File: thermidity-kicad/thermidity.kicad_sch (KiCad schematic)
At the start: 14 parts, among them J1 Battery, J2 Display, J3 ISP, U1 ATmega328P, U2 HIH-5030, U3 TMP36

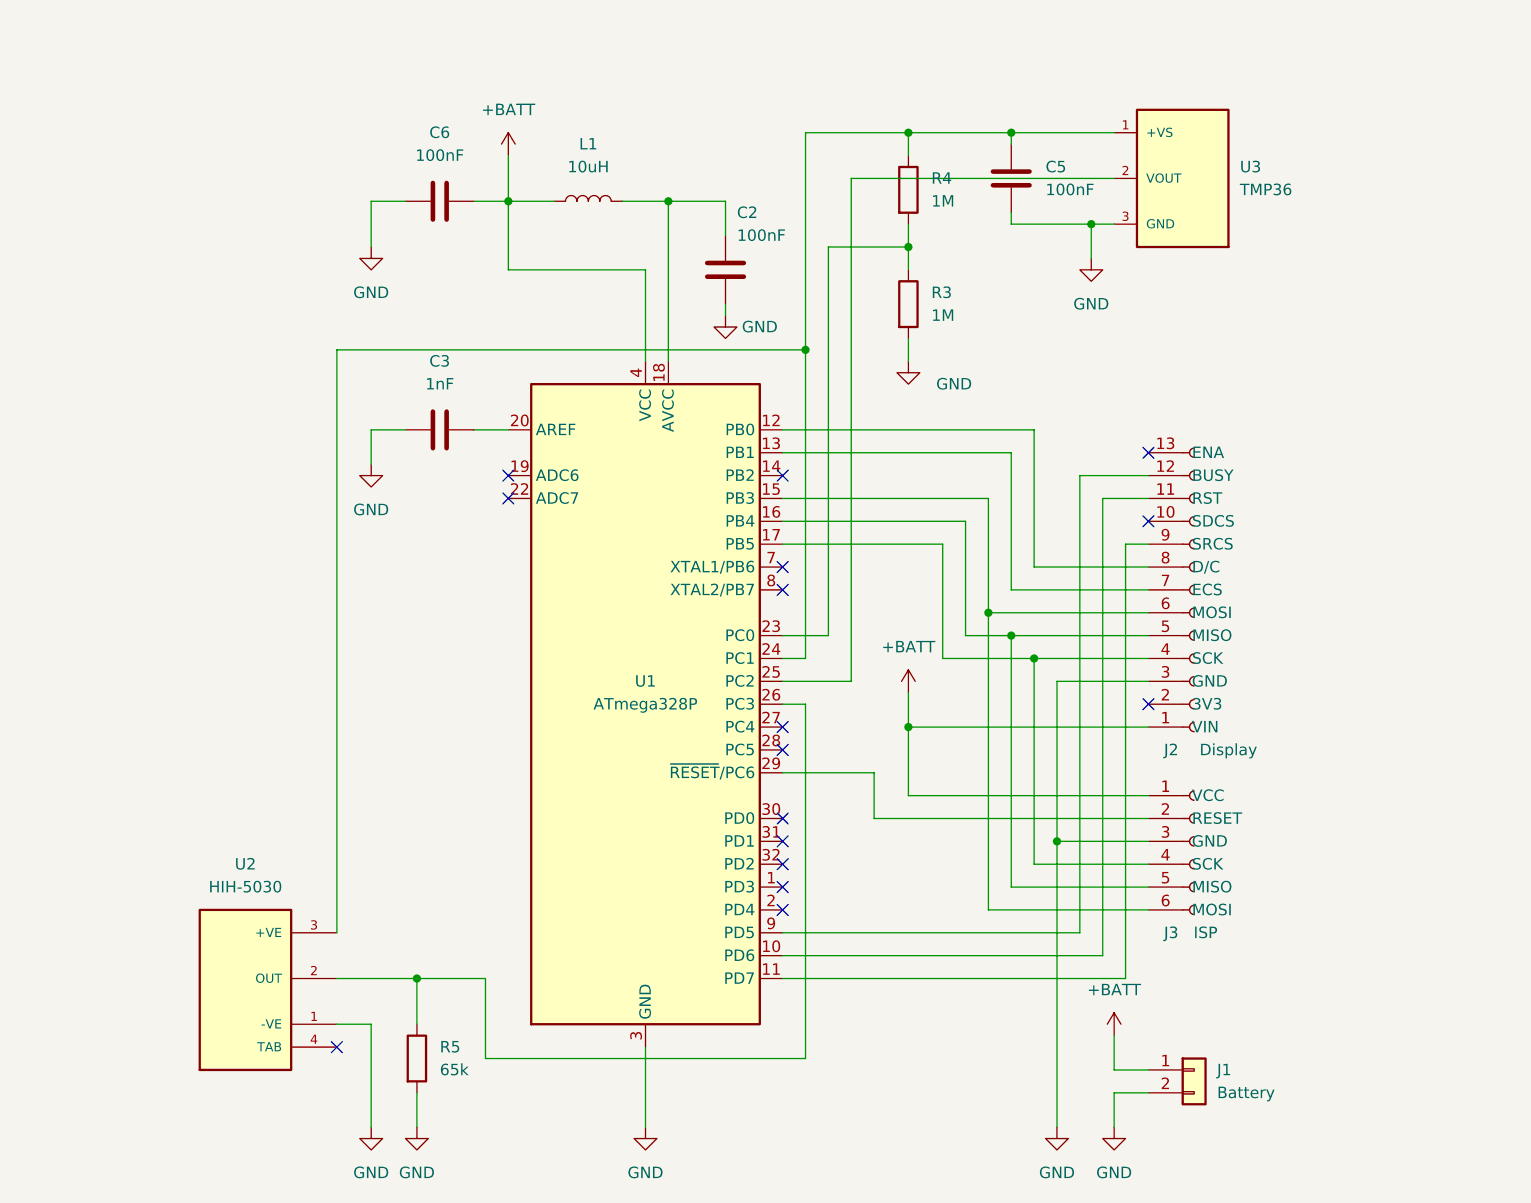
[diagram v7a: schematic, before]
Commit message: remove the 1pF capacitor between AREF and GND
- takes ~125us to discharge after switching from AVCC to internal 1.1 voltage reference and for the reference to settle
- shouldn't be necessary and hopefully the 16x oversampling benefits from some noise
- one part less
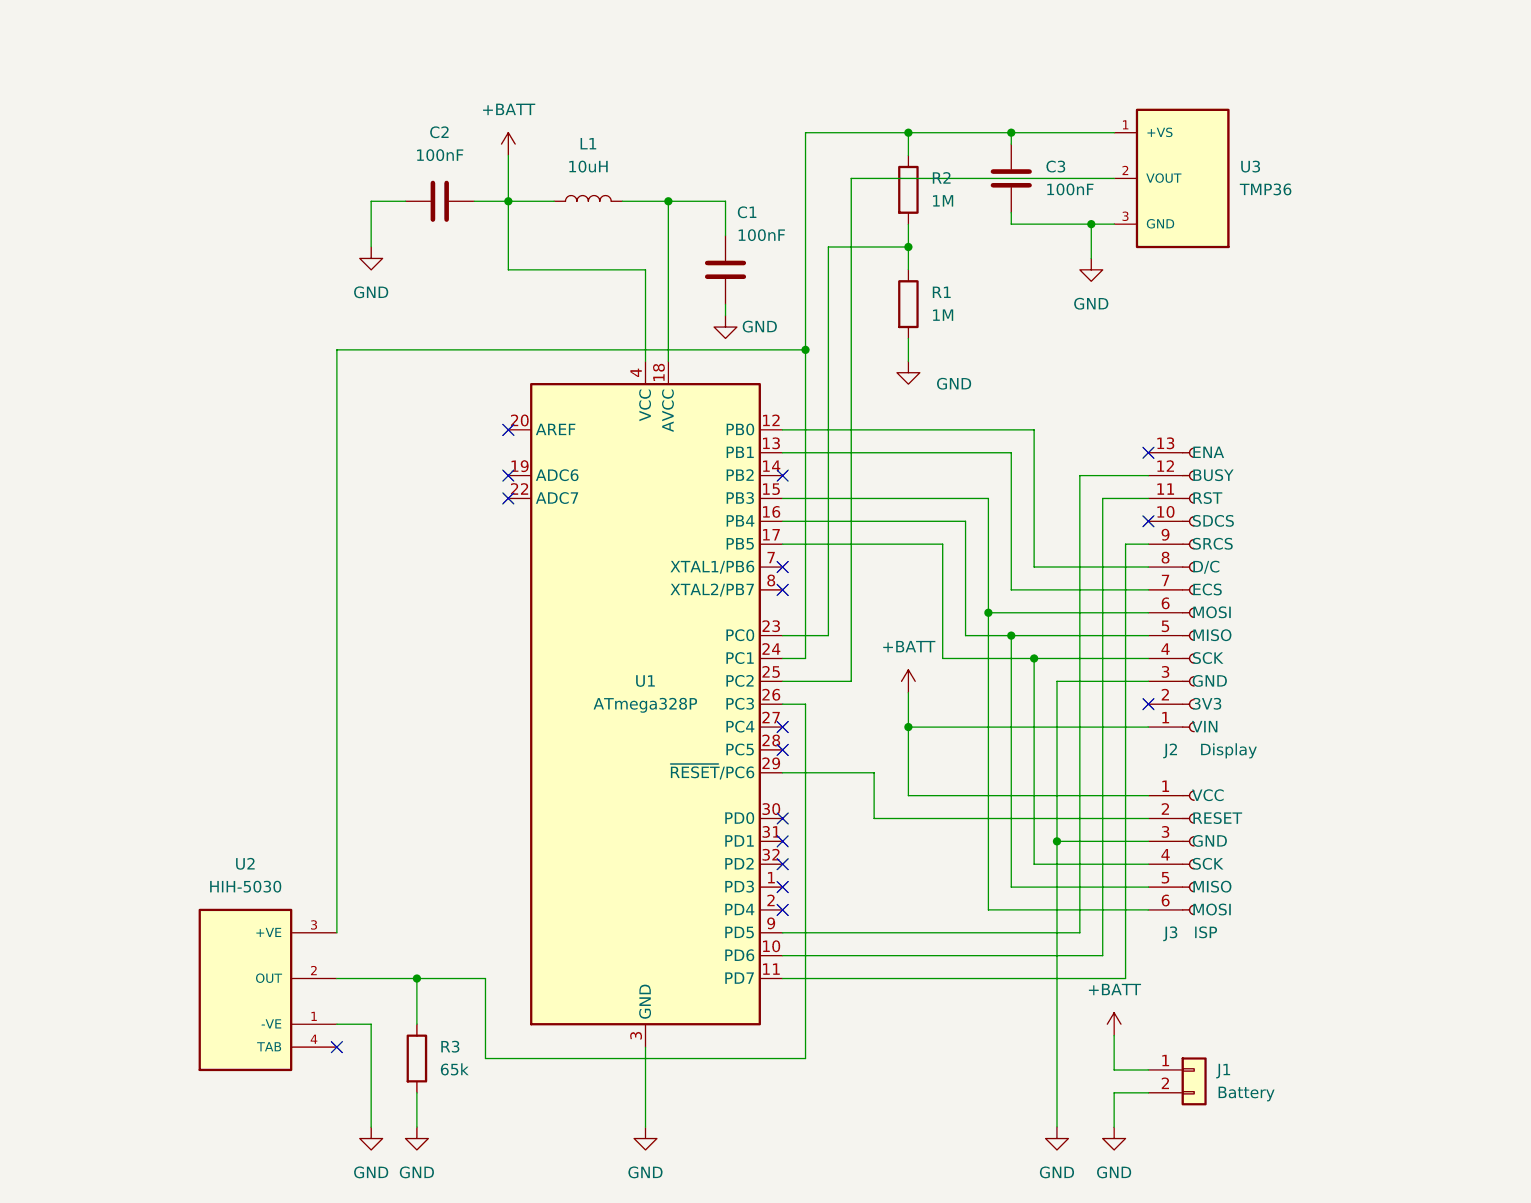
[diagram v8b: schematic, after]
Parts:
- removed C3: 1nF, Capacitor_SMD:C_1206_3216Metric_Pad1.33x1.80mm_HandSolder, symbol Device:C
- renumbered C2 to C1, C6 to C2, C5 to C3, R3 to R1, R4 to R2, R5 to R3
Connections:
- no-connect marks 16 -> 17
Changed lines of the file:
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@@
   (no_connect (at 161.29 101.6))
   (no_connect (at 161.29 116.84))
+  (no_connect (at 130.81 66.04))
   (no_connect (at 161.29 114.3))
   (no_connect (at 161.29 99.06))
@@
     (stroke (width 0) (type default) (color 0 0 0 0))
   )
-  (wire (pts (xy 127 66.04) (xy 130.81 66.04))
-    (stroke (width 0) (type default) (color 0 0 0 0))
-  )
   (wire (pts (xy 161.29 73.66) (xy 184.15 73.66))
     (stroke (width 0) (type default) (color 0 0 0 0))
@@
     (stroke (width 0) (type default) (color 0 0 0 0))
   )
-  (wire (pts (xy 119.38 66.04) (xy 115.57 66.04))
-    (stroke (width 0) (type default) (color 0 0 0 0))
-  )
   (wire (pts (xy 143.51 40.64) (xy 148.59 40.64))
     (stroke (width 0) (type default) (color 0 0 0 0))
@@
     (stroke (width 0) (type default) (color 0 0 0 0))
   )
-  (wire (pts (xy 115.57 66.04) (xy 115.57 69.85))
-    (stroke (width 0) (type default) (color 0 0 0 0))
-  )
   (wire (pts (xy 120.65 127) (xy 128.27 127))
     (stroke (width 0) (type default) (color 0 0 0 0))
@@
   (symbol (lib_id "Device:C") (at 186.69 38.1 0) (unit 1)
     (in_bom yes) (on_board yes) (fields_autoplaced)
-    (property "Reference" "C5" (id 0) (at 190.5 36.8299 0)
+    (property "Reference" "C3" (id 0) (at 190.5 36.8299 0)
       (effects (font (size 1.27 1.27)) (justify left))
     )
@@
   (symbol (lib_id "Device:C") (at 123.19 40.64 90) (unit 1)
     (in_bom yes) (on_board yes) (fields_autoplaced)
-    (property "Reference" "C6" (id 0) (at 123.19 33.02 90))
+    (property "Reference" "C2" (id 0) (at 123.19 33.02 90))
     (property "Value" "100nF" (id 1) (at 123.19 35.56 90))
     (property "Footprint" "Capacitor_SMD:C_1206_3216Metric_Pad1.33x1.80mm_HandSolder" (id 2) (at 127 39.6748 0)
@@
   (symbol (lib_id "Device:C") (at 154.94 48.26 180) (unit 1)
     (in_bom yes) (on_board yes)
-    (property "Reference" "C2" (id 0) (at 156.21 41.91 0)
+    (property "Reference" "C1" (id 0) (at 156.21 41.91 0)
       (effects (font (size 1.27 1.27)) (justify right))
     )
@@
     (pin "1")
   )
-  (symbol (lib_id "power:GND") (at 115.57 69.85 0) (unit 1)
-    (in_bom yes) (on_board yes) (fields_autoplaced)
-    (property "Reference" "#PWR0102" (id 0) (at 115.57 76.2 0)
-      (effects (font (size 1.27 1.27)) hide)
-    )
-    (property "Value" "GND" (id 1) (at 115.57 74.93 0))
-    (property "Footprint" "" (id 2) (at 115.57 69.85 0)
-      (effects (font (size 1.27 1.27)) hide)
-    )
-    (property "Datasheet" "" (id 3) (at 115.57 69.85 0)
-      (effects (font (size 1.27 1.27)) hide)
-    )
-    (pin "1")
-  )
   (symbol (lib_id "Device:R") (at 120.65 135.89 0) (unit 1)
     (in_bom yes) (on_board yes) (fields_autoplaced)
-    (property "Reference" "R5" (id 0) (at 123.19 134.6199 0)
+    (property "Reference" "R3" (id 0) (at 123.19 134.6199 0)
       (effects (font (size 1.27 1.27)) (justify left))
     )
@@
   (symbol (lib_id "Device:R") (at 175.26 52.07 0) (unit 1)
     (in_bom yes) (on_board yes) (fields_autoplaced)
-    (property "Reference" "R3" (id 0) (at 177.8 50.7999 0)
+    (property "Reference" "R1" (id 0) (at 177.8 50.7999 0)
       (effects (font (size 1.27 1.27)) (justify left))
     )
@@
   (symbol (lib_id "Device:R") (at 175.26 39.37 0) (unit 1)
     (in_bom yes) (on_board yes) (fields_autoplaced)
-    (property "Reference" "R4" (id 0) (at 177.8 38.0999 0)
+    (property "Reference" "R2" (id 0) (at 177.8 38.0999 0)
       (effects (font (size 1.27 1.27)) (justify left))
     )
@@
     )
     (property "Datasheet" "~" (id 3) (at 175.26 39.37 0)
-      (effects (font (size 1.27 1.27)) hide)
-    )
-    (pin "1")
-    (pin "2")
-  )
-  (symbol (lib_id "Device:C") (at 123.19 66.04 90) (unit 1)
-    (in_bom yes) (on_board yes) (fields_autoplaced)
-    (property "Reference" "C3" (id 0) (at 123.19 58.42 90))
-    (property "Value" "1nF" (id 1) (at 123.19 60.96 90))
-    (property "Footprint" "Capacitor_SMD:C_1206_3216Metric_Pad1.33x1.80mm_HandSolder" (id 2) (at 127 65.0748 0)
-      (effects (font (size 1.27 1.27)) hide)
-    )
-    (property "Datasheet" "~" (id 3) (at 123.19 66.04 0)
       (effects (font (size 1.27 1.27)) hide)
     )
@@
       (reference "#PWR0101") (unit 1) (value "GND") (footprint "")
     )
-    (path "/c88d99c3-9206-4775-bf42-a9352b3209c2"
-      (reference "#PWR0102") (unit 1) (value "GND") (footprint "")
-    )
     (path "/020ac1ad-0160-4ab9-a9f1-55e79d05e91a"
       (reference "#PWR0104") (unit 1) (value "GND") (footprint "")
@@
     )
     (path "/afc68921-ea8b-403a-9e3b-f2ef0af928a6"
+      (reference "C1") (unit 1) (value "100nF") (footprint "Capacitor_SMD:C_1206_3216Metric_Pad1.33x1.80mm_HandSolder")
+    )
+    (path "/8e459bfb-75fb-4c36-90af-73c840018779"
       (reference "C2") (unit 1) (value "100nF") (footprint "Capacitor_SMD:C_1206_3216Metric_Pad1.33x1.80mm_HandSolder")
     )
-    (path "/fb41d1b8-7978-4471-8222-322ad33b566c"
-      (reference "C3") (unit 1) (value "1nF") (footprint "Capacitor_SMD:C_1206_3216Metric_Pad1.33x1.80mm_HandSolder")
-    )
     (path "/0178a398-4cac-462d-a5f8-54e853b1fa89"
-      (reference "C5") (unit 1) (value "100nF") (footprint "Capacitor_SMD:C_1206_3216Metric_Pad1.33x1.80mm_HandSolder")
-    )
-    (path "/8e459bfb-75fb-4c36-90af-73c840018779"
-      (reference "C6") (unit 1) (value "100nF") (footprint "Capacitor_SMD:C_1206_3216Metric_Pad1.33x1.80mm_HandSolder")
+      (reference "C3") (unit 1) (value "100nF") (footprint "Capacitor_SMD:C_1206_3216Metric_Pad1.33x1.80mm_HandSolder")
     )
     (path "/346b2658-5c55-45ae-8c48-4ce2f357fb5f"
@@
     )
     (path "/d690645f-ce9c-4e4e-9a40-30e90181925c"
-      (reference "R3") (unit 1) (value "1M") (footprint "Resistor_SMD:R_0805_2012Metric_Pad1.20x1.40mm_HandSolder")
+      (reference "R1") (unit 1) (value "1M") (footprint "Resistor_SMD:R_0805_2012Metric_Pad1.20x1.40mm_HandSolder")
     )
     (path "/f5367a98-6a53-432b-8730-086e1bb8663c"
-      (reference "R4") (unit 1) (value "1M") (footprint "Resistor_SMD:R_0805_2012Metric_Pad1.20x1.40mm_HandSolder")
+      (reference "R2") (unit 1) (value "1M") (footprint "Resistor_SMD:R_0805_2012Metric_Pad1.20x1.40mm_HandSolder")
     )
     (path "/ce63e81c-5d78-4d98-bb9e-4b0f5b9f1c49"
-      (reference "R5") (unit 1) (value "65k") (footprint "Resistor_SMD:R_0805_2012Metric_Pad1.20x1.40mm_HandSolder")
+      (reference "R3") (unit 1) (value "65k") (footprint "Resistor_SMD:R_0805_2012Metric_Pad1.20x1.40mm_HandSolder")
     )
     (path "/a564f624-0149-43d3-9b25-20abc178b1e7"
